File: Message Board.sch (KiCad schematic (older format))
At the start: 40 parts, among them J1 Conn_01x02, Q1 LGE2300, Q2 LGE2300, SW1 SW_SPST, U1 esp32-c3, U2 LM1117-5.0, U3 LM1117-3.3, U4 epaper75

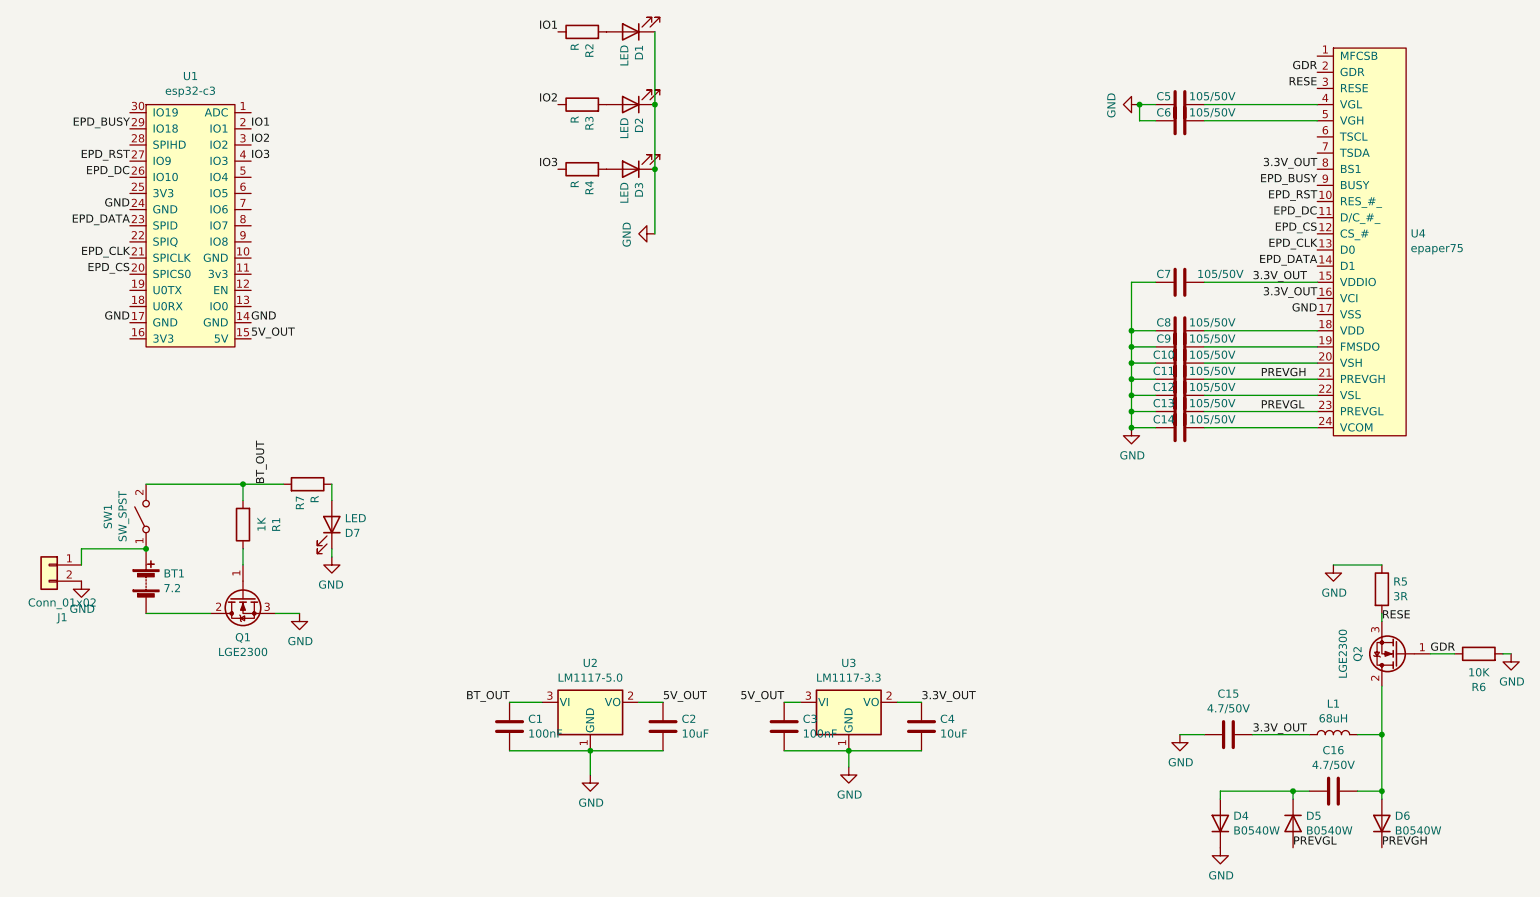
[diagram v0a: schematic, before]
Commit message: Changed orientation of the FFC connector, battery from 2x18650 to 1x18650, devboard to ESP32-C3-DEVKITM-1 and updated the epaper footprint. Deleted second linear regualtor
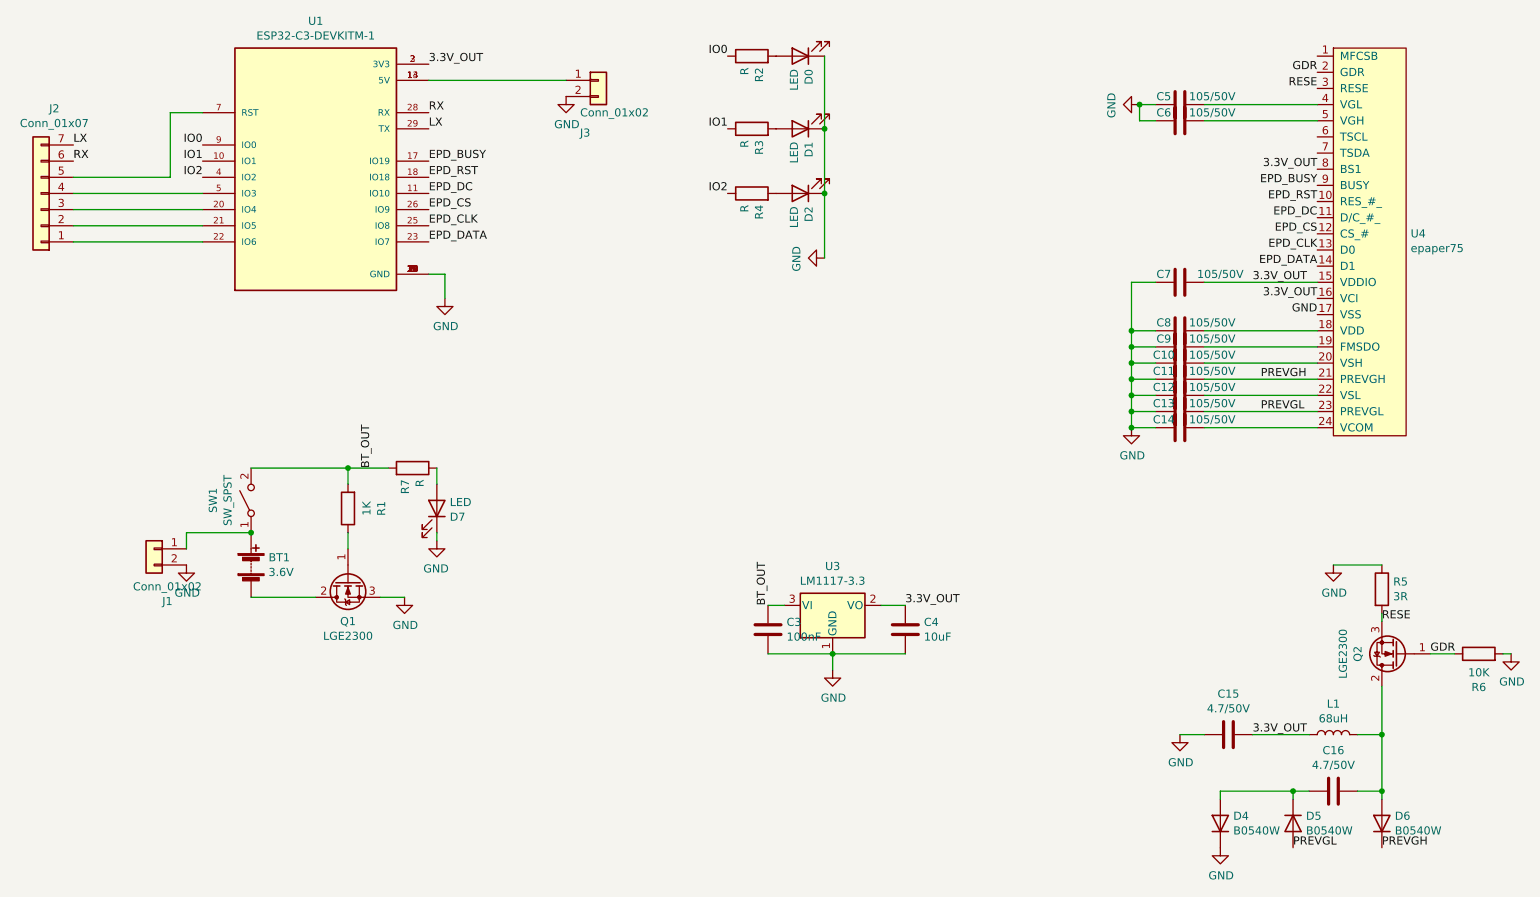
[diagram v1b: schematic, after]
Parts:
- removed C1: 100nF, Capacitor_SMD:C_1206_3216Metric_Pad1.33x1.80mm_HandSolder, symbol Device:C
- removed C2: 10uF, Capacitor_SMD:C_1206_3216Metric_Pad1.33x1.80mm_HandSolder, symbol Device:C
- removed U1: esp32-c3, jw_lib:esp32-c3-s32-footprint, symbol Message-Board-rescue:esp32-c3-jw_library
- removed U2: LM1117-5.0, Package_TO_SOT_SMD:SOT-223, symbol Regulator_Linear:LM1117-5.0
- added J2: Conn_01x07, Connector_JST:JST_EH_S7B-EH_1x07_P2.50mm_Horizontal, symbol Connector_Generic:Conn_01x07
- added J3: Conn_01x02, Connector_JST:JST_EH_S2B-EH_1x02_P2.50mm_Horizontal, symbol Connector_Generic:Conn_01x02
- added U1: ESP32-C3-DEVKITM-1, jw_lib:XCVR_ESP32-C3-DEVKITM-1, symbol ESP32-C3-DEVKITM-1:ESP32-C3-DEVKITM-1
- BT1: value 7.2 -> 3.6V; footprint Battery:BatteryHolder_Keystone_2462_2xAA -> Battery:BatteryHolder_Keystone_1042_1x18650
- L1: footprint Inductor_SMD:L_1206_3216Metric_Pad1.22x1.90mm_HandSolder -> Inductor_SMD:L_12x12mm_H6mm
- SW1: footprint Button_Switch_THT:SW_DIP_SPSTx01_Slide_9.78x4.72mm_W7.62mm_P2.54mm -> (none)
- renumbered D1 to D0, D2 to D1, D3 to D2
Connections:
- net 5V_OUT is gone; now on net BT_OUT: C3.1, U3.3 (VI)
- net IO3 is gone; now on net IO2: R4.1
- net 3.3V_OUT: now also U1.2 (3V3), U1.3 (3V3)
- net EPD_BUSY: now also U1.17 (IO19)
- net EPD_CLK: now also U1.25 (IO8)
- net EPD_CS: now also U1.26 (IO9)
- net EPD_DATA: now also U1.23 (IO7)
- net EPD_DC: now also U1.11 (IO10)
- net EPD_RST: now also U1.18 (IO18)
- net GND: now also J3.2 (Pin_2), U1.1 (GND), U1.12 (GND), U1.15 (GND), U1.16 (GND), U1.19 (GND), U1.24 (GND), U1.27 (GND), U1.30 (GND), U1.6 (GND), U1.8 (GND)
- net IO1: now also R3.1, U1.10 (IO1); no longer R2.1
- net IO2: now also U1.4 (IO2); no longer R3.1
- new net: J3.1 (Pin_1), U1.13 (5V), U1.14 (5V)
- new net: J2.3 (Pin_3), U1.20 (IO4)
- new net: J2.2 (Pin_2), U1.21 (IO5)
- new net: J2.1 (Pin_1), U1.22 (IO6)
- new net: J2.4 (Pin_4), U1.5 (IO3)
- new net: J2.5 (Pin_5), U1.7 (RST)
- new net IO0: R2.1, U1.9 (IO0)
- new net LX: J2.7 (Pin_7), U1.29 (TX)
- new net RX: J2.6 (Pin_6), U1.28 (RX)
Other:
- moved on the sheet: BT1, C3, C4, D0, D1, D2, D7, J1, Q1, R1, R2, R3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

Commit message: Updated SPI connections, added hardware possibility to chose if 3 or 4 SPI version (BS Pin)
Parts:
- added J4: Conn_01x03, Connector_JST:JST_EH_B3B-EH-A_1x03_P2.50mm_Vertical, symbol Connector_Generic:Conn_01x03
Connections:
- net 3.3V_OUT: now also J4.3 (Pin_3); no longer U4.8 (BS1)
- net EPD_BUSY: now also U1.5 (IO3); no longer U1.17 (IO19)
- net EPD_CLK: now also U1.22 (IO6); no longer U1.25 (IO8)
- net EPD_CS: now also U1.11 (IO10); no longer U1.26 (IO9)
- net EPD_DC: now also U1.25 (IO8); no longer U1.11 (IO10)
- net EPD_RST: now also U1.26 (IO9); no longer U1.18 (IO18)
- net GND: now also J4.1 (Pin_1)
- net IO18: now reaches J2.3 (Pin_3)
- net IO18: now also U1.18 (IO18); no longer U1.20 (IO4)
- net IO5: now reaches J2.2 (Pin_2), U1.21 (IO5)
- net IO4: now reaches J2.1 (Pin_1)
- net IO4: now also U1.20 (IO4); no longer U1.22 (IO6)
- net IO19: now reaches J2.4 (Pin_4)
- net IO19: now also U1.17 (IO19); no longer U1.5 (IO3)
- net RST: now reaches J2.5 (Pin_5), U1.7 (RST)
- new net BS: J4.2 (Pin_2), U4.8 (BS1)
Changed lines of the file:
@@
 Text Label 8900 1900 2    50   ~ 0
 EPD_BUSY
-Text Label 8900 1800 2    50   ~ 0
+Text Label 6000 3150 0    50   ~ 0
 3.3V_OUT
 Text Label 8900 1300 2    50   ~ 0
@@
 Text Label 2000 1850 2    50   ~ 0
 IO2
-Text Label 3400 1750 0    50   ~ 0
+Text Label 2000 1950 2    50   ~ 0
 EPD_BUSY
-Text Label 3400 1850 0    50   ~ 0
+Text Label 3400 2050 0    50   ~ 0
 EPD_RST
+Text Label 3400 2150 0    50   ~ 0
+EPD_DC
 Text Label 3400 1950 0    50   ~ 0
-EPD_DC
-Text Label 3400 2050 0    50   ~ 0
 EPD_CS
-Text Label 3400 2150 0    50   ~ 0
+Text Label 2000 2250 2    50   ~ 0
 EPD_CLK
 Text Label 3400 2250 0    50   ~ 0
@@
 	-1   0    0    1
 $EndComp
-Wire Wire Line
-	2000 2250 1200 2250
-Wire Wire Line
-	2000 2150 1200 2150
-Wire Wire Line
-	1200 2050 2000 2050
-Wire Wire Line
-	2000 1950 1200 1950
-Wire Wire Line
-	1200 1850 1800 1850
-Wire Wire Line
-	1800 1850 1800 1450
-Wire Wire Line
-	1800 1450 2000 1450
 Text Label 3400 1450 0    50   ~ 0
 RX
@@
 Text Label 1200 1750 0    50   ~ 0
 RX
+Text Label 3400 1850 0    50   ~ 0
+IO18
+Text Label 1200 2050 0    50   ~ 0
+IO18
+Text Label 3400 1750 0    50   ~ 0
+IO19
+Text Label 1200 1950 0    50   ~ 0
+IO19
+Text Label 2000 1450 2    50   ~ 0
+RST
+Text Label 1200 1850 0    50   ~ 0
+RST
+Text Label 2000 2050 2    50   ~ 0
+IO4
+Text Label 1200 2250 0    50   ~ 0
+IO4
+Text Label 2000 2150 2    50   ~ 0
+IO5
+Text Label 1200 2150 0    50   ~ 0
+IO5
+$Comp
+L Connector_Generic:Conn_01x03 J4
+U 1 1 62136BF1
+P 5800 3250
+F 0 "J4" H 5718 2925 50  0000 C CNN
+F 1 "Conn_01x03" H 5718 3016 50  0000 C CNN
+F 2 "Connector_JST:JST_EH_B3B-EH-A_1x03_P2.50mm_Vertical" H 5800 3250 50  0001 C CNN
+F 3 "~" H 5800 3250 50  0001 C CNN
+	1    5800 3250
+	-1   0    0    1
+$EndComp
+$Comp
+L power:GND #PWR0114
+U 1 1 62137F60
+P 6100 3350
+F 0 "#PWR0114" H 6100 3100 50  0001 C CNN
+F 1 "GND" H 6105 3177 50  0000 C CNN
+F 2 "" H 6100 3350 50  0001 C CNN
+F 3 "" H 6100 3350 50  0001 C CNN
+	1    6100 3350
+	1    0    0    -1
+$EndComp
+Wire Wire Line
+	6100 3350 6000 3350
+Text Label 6000 3250 0    50   ~ 0
+BS
+Text Label 8900 1800 2    50   ~ 0
+BS
 $EndSCHEMATC
